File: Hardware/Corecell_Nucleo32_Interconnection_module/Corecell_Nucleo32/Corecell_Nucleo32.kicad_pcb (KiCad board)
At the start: 2 copper layers, 166.3 x 92.6 mm, 30 parts, among them IC1 PCI_EXPRESS_CARD, J1 Conn_01x19, J2 Conn_01x19, J3 Bus Standard, J4 Calculatrice_UART_groove, J5 RAK5146_UART_groove(GPS), J6 RAK5146_I2C_groove(GPS), J7 RAK5146_SPI_groove(MCU), Q1 BC548, U1 ESP32-DEVKITC-32D

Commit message: Design changed
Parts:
- moved C6 153.3 mm to (175.3, 43.9), turned to 90 degrees
- moved C2 141.3 mm to (163.0, 40.3), turned to -90 degrees
- moved C3 134.7 mm to (163.0, 48.7), turned to 90 degrees
- moved J4 127.9 mm to (184.5, 119.0), turned to 90 degrees
- moved C1 124.1 mm to (162.7, 52.3), turned to -90 degrees
- moved C8 118.6 mm to (161.5, 96.0), turned to 90 degrees
- moved R1 118.0 mm to (180.8, 78.4), turned to 90 degrees
- moved C4 116.5 mm to (175.3, 45.8), turned to -90 degrees
- moved R4 112.8 mm to (140.0, 59.9), turned to 90 degrees
- moved R8 106.4 mm to (137.1, 86.9), turned to 180 degrees
- moved R6 101.1 mm to (149.8, 102.3), turned to 90 degrees
- moved R3 92.5 mm to (172.8, 73.2), turned to 90 degrees
- moved IC1 88.9 mm to (169.3, 51.4)
- moved C5 87.1 mm to (163.0, 62.7), turned to 90 degrees
- moved R2 86.6 mm to (169.0, 69.3), turned to 90 degrees
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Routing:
- net +3V3: track 0.00 -> 46.7 mm
- net GND: track 0.00 -> 41.3 mm
- net /8: track 0.00 -> 8.50 mm
- net /5: track 0.00 -> 8.50 mm
- net /31: track 0.00 -> 8.50 mm
- net /27: track 0.00 -> 8.50 mm
- net /24: track 0.00 -> 8.50 mm
- net /12: track 0.00 -> 8.50 mm
- net /37: track 0.00 -> 8.50 mm
- net /35: track 0.00 -> 8.50 mm
- net /34: track 0.00 -> 8.50 mm
- net /18: track 0.00 -> 8.50 mm
- net /16: track 0.00 -> 8.50 mm
- net /15: track 0.00 -> 8.50 mm
- net /19: track 0.00 -> 8.50 mm
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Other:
- board text added: "NUCLEO32"
- board text added: "RAK5146"

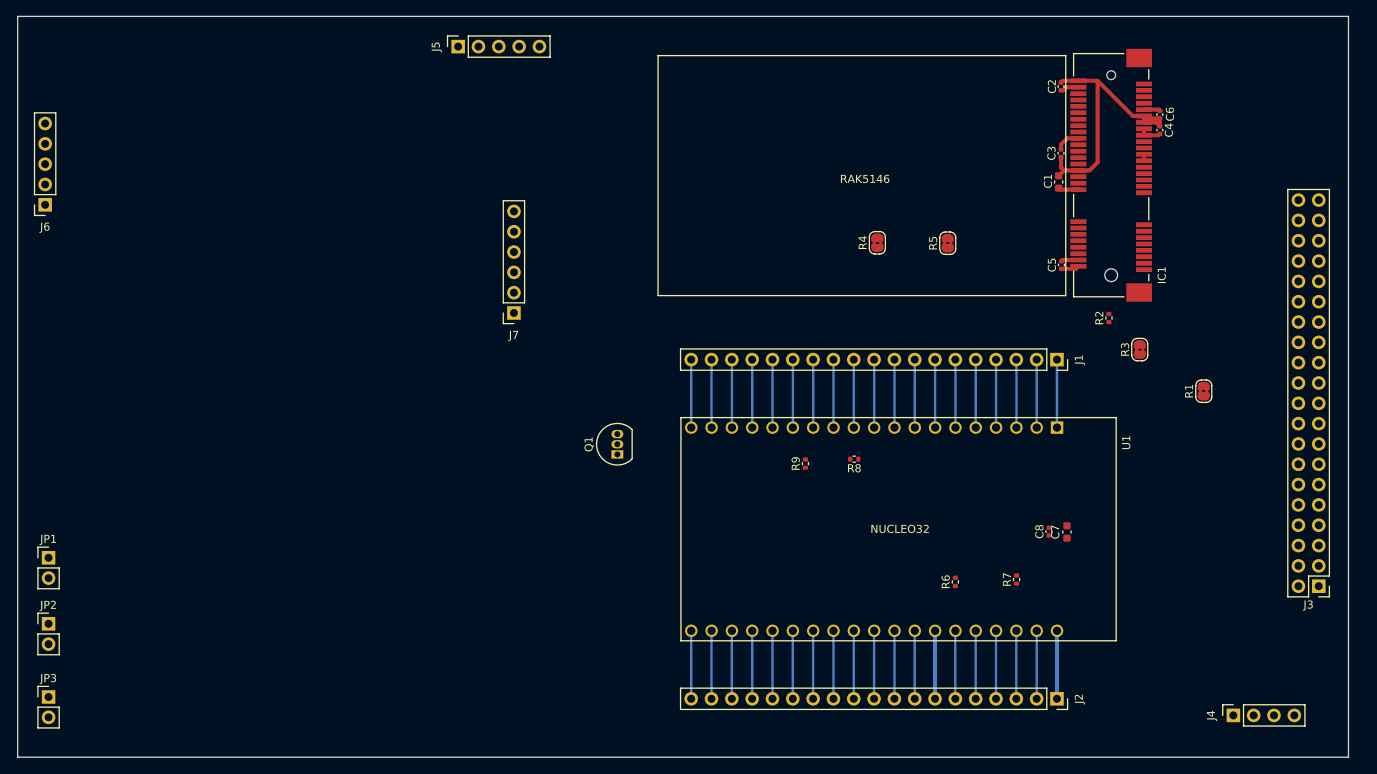
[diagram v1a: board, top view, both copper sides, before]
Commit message: Some changes in footprint and capacitors value
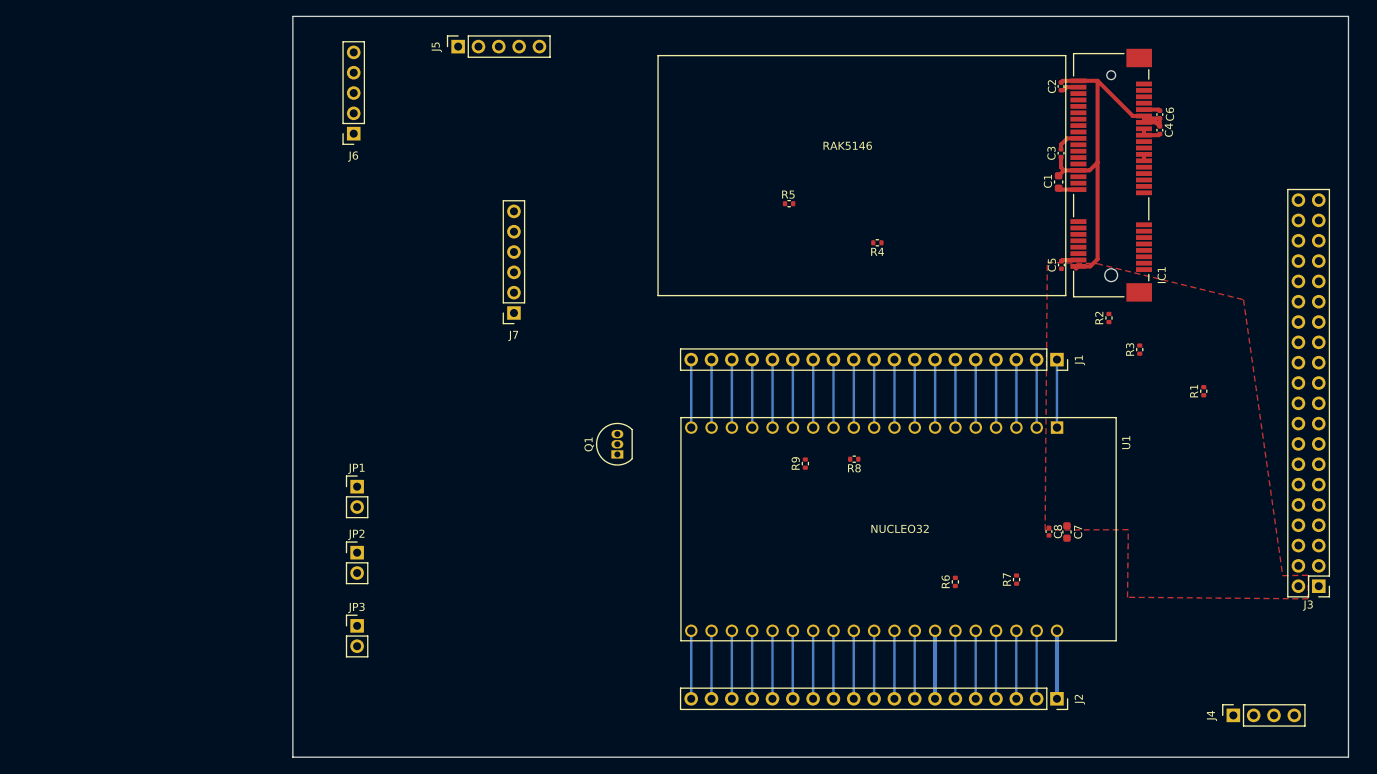
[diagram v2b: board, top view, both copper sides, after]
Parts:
- R1, R3: footprint Jumper:SolderJumper-2_P1.3mm_Bridged2Bar_RoundedPad1.0x1.5mm -> Resistor_SMD:R_0402_1005Metric
- R4, R5: value 0/NC -> 0; footprint Jumper:SolderJumper-2_P1.3mm_Bridged2Bar_RoundedPad1.0x1.5mm -> Resistor_SMD:R_0402_1005Metric
- R6, R7, R9: value 100/NC -> 100
- moved J6 39.6 mm to (74.6, 46.2)
- moved JP1 39.6 mm to (75.0, 90.4)
- moved JP2 39.6 mm to (75.0, 98.6)
- moved JP3 39.6 mm to (75.0, 107.8)
- moved R5 20.4 mm to (129.0, 55.0), turned to 180 degrees
- turned C7 to -90 degrees
- turned C8 to -90 degrees
- turned R4 to 180 degrees
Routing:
- net +3V3: track 46.7 -> 59.8 mm
- added copper zone on F.Cu, net +3V3
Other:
- board size 166.3 x 92.6 mm -> 131.9 x 92.6 mm

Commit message: Model is ready. We must revise
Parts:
- R1, R2, R4, R5: moved to B.Cu
- moved JP3 111.4 mm to (186.4, 110.2)
- moved JP1 107.2 mm to (180.4, 109.9)
- moved JP2 101.3 mm to (175.7, 109.9)
- moved J4 85.1 mm to (102.5, 96.0), turned to 0 degrees
- moved J6 51.1 mm to (102.5, 89.0)
- moved J5 40.1 mm to (102.5, 72.5), turned to 180 degrees
- moved R2 26.8 mm to (142.2, 70.9)
- moved R3 25.6 mm to (147.3, 71.4)
- moved R5 16.3 mm to (134.4, 70.4), turned to -90 degrees
- moved J7 15.8 mm to (102.5, 55.0)
- moved R8 13.4 mm to (126.9, 95.5), turned to 90 degrees
- moved R4 10.9 mm to (137.2, 70.4), turned to -90 degrees
- moved R1 5.73 mm to (186.6, 78.0)
- moved Q1 4.86 mm to (110.5, 90.2)
- moved R9 4.11 mm to (131.9, 91.5), turned to 0 degrees
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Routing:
- net /28: track 8.50 -> 230.1 mm, vias 0 -> 1
- net /21: track 8.50 -> 186.8 mm, vias 0 -> 1
- net /24: track 8.50 -> 180.1 mm, vias 0 -> 2
- net /23: track 8.50 -> 159.6 mm, vias 0 -> 1
- net /29: track 8.50 -> 154.9 mm
- net /31: track 8.50 -> 150.9 mm
- net /27: track 8.50 -> 146.4 mm, vias 0 -> 1
- net /30: track 8.50 -> 144.3 mm
- net +3V3: track 59.8 -> 176.1 mm, vias 0 -> 3
- net /8: track 8.50 -> 114.9 mm, vias 0 -> 1
- net Net-(IC1-Pad22): track 0.00 -> 91.2 mm, vias 0 -> 2
- net /6: track 8.50 -> 95.5 mm
- net /9: track 8.50 -> 84.1 mm, vias 0 -> 3
- net /22: track 8.50 -> 79.5 mm, vias 0 -> 1
- net Net-(IC1-Pad30): track 0.00 -> 68.3 mm, vias 0 -> 2
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- added copper zone on B.Cu, net GND
- added copper zone on F.Cu, net GND
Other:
- board size 131.9 x 92.6 mm -> 102 x 92.6 mm

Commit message: Silk screen is up to date
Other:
- board text added: "3V3"
- board text added: "CS"
- board text added: "GND"
- board text added: "GPS PULSE"
- board text added: "I2C GPS"
- board text added: "MISO"
- board text added: "MOSI"
- board text added: "RESET GPS"
- board text added: "RESET MCU RAK"
- board text added: "RX"
- board text added: "RX GPS"
- board text added: "SCK"
- board text added: "SCL"
- board text added: "SDA"
- board text added: "SPI MCU RAK"
- board text added: "STDBY GPS"
- board text added: "TX"
- board text added: "TX GPS"
- board text added: "UART GPS"
- board text added: "UART OBS"
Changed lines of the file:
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@@
     (property "Sheetname" "")
     (attr through_hole)
-    (fp_text reference "J4" (at 0 -2.77) (layer "F.SilkS")
+    (fp_text reference "J4" (at 0 10) (layer "F.SilkS")
       (effects (font (size 1 1) (thickness 0.15)))
     )
@@
     (property "Sheetname" "")
     (attr through_hole)
-    (fp_text reference "J5" (at 0 -2.77) (layer "F.SilkS")
+    (fp_text reference "J5" (at 0 -2.45) (layer "F.SilkS")
       (effects (font (size 1 1) (thickness 0.15)))
     )
@@
     (property "Sheetname" "")
     (attr through_hole)
-    (fp_text reference "J7" (at 0 -2.77) (layer "F.SilkS")
+    (fp_text reference "J7" (at 0 -2.5) (layer "F.SilkS")
       (effects (font (size 1 1) (thickness 0.15)))
     )
@@
     (property "Sheetname" "")
     (attr through_hole)
-    (fp_text reference "J6" (at 0 -2.77) (layer "F.SilkS")
+    (fp_text reference "J6" (at 0 -2.5) (layer "F.SilkS")
       (effects (font (size 1 1) (thickness 0.15)))
     )
@@
   (gr_rect (start 112.62 66.49) (end 163.58 36.49) (layer "F.SilkS") (width 0.15) (fill none))
   (gr_rect (start 98.42 31.59) (end 200.436 124.19) (layer "Edge.Cuts") (width 0.1) (fill none))
+  (gr_text "GPS PULSE\n" (at 106.5 81.5) (layer "F.SilkS")
+    (effects (font (size 0.5 0.5) (thickness 0.125)))
+  )
+  (gr_text "UART OBS" (at 103 108) (layer "F.SilkS")
+    (effects (font (size 1 1) (thickness 0.15)))
+  )
+  (gr_text "UART GPS\n" (at 103 76.5) (layer "F.SilkS")
+    (effects (font (size 1 1) (thickness 0.15)))
+  )
+  (gr_text "GND" (at 105 79) (layer "F.SilkS")
+    (effects (font (size 0.5 0.5) (thickness 0.125)))
+  )
+  (gr_text "SCL" (at 105 86.5) (layer "F.SilkS")
+    (effects (font (size 0.5 0.5) (thickness 0.125)))
+  )
+  (gr_text "RX" (at 105 98.5) (layer "F.SilkS")
+    (effects (font (size 0.5 0.5) (thickness 0.125)))
+  )
+  (gr_text "RX GPS" (at 106 67.5) (layer "F.SilkS")
+    (effects (font (size 0.5 0.5) (thickness 0.125)))
+  )
+  (gr_text "GND" (at 105 103.5) (layer "F.SilkS")
+    (effects (font (size 0.5 0.5) (thickness 0.125)))
+  )
+  (gr_text "STDBY GPS\n" (at 175 114.5) (layer "F.SilkS")
+    (effects (font (size 0.5 0.5) (thickness 0.125)))
+  )
   (gr_text "NUCLEO32\n" (at 142.87 95.69) (layer "F.SilkS")
     (effects (font (size 1 1) (thickness 0.15)))
   )
+  (gr_text "GND" (at 105 42.5) (layer "F.SilkS")
+    (effects (font (size 0.5 0.5) (thickness 0.125)))
+  )
+  (gr_text "3V3\n" (at 105 96) (layer "F.SilkS")
+    (effects (font (size 0.5 0.5) (thickness 0.125)))
+  )
+  (gr_text "SCK\n" (at 105 52.5) (layer "F.SilkS")
+    (effects (font (size 0.5 0.5) (thickness 0.125)))
+  )
   (gr_text "RAK5146\n" (at 136.3 47.8) (layer "F.SilkS")
     (effects (font (size 1 1) (thickness 0.15)))
   )
+  (gr_text "MISO\n" (at 105 50) (layer "F.SilkS")
+    (effects (font (size 0.5 0.5) (thickness 0.125)))
+  )
+  (gr_text "GPS PULSE\n" (at 106.5 65) (layer "F.SilkS")
+    (effects (font (size 0.5 0.5) (thickness 0.125)))
+  )
+  (gr_text "RESET GPS" (at 180.5 114.5) (layer "F.SilkS")
+    (effects (font (size 0.5 0.5) (thickness 0.125)))
+  )
+  (gr_text "3V3\n" (at 105.5 72.888944) (layer "F.SilkS")
+    (effects (font (size 0.5 0.5) (thickness 0.125)))
+  )
+  (gr_text "3V3\n" (at 105 89) (layer "F.SilkS")
+    (effects (font (size 0.5 0.5) (thickness 0.125)))
+  )
+  (gr_text "RESET MCU RAK" (at 186.4 114.5) (layer "F.SilkS")
+    (effects (font (size 0.5 0.5) (thickness 0.125)))
+  )
+  (gr_text "TX" (at 105.130233 100.79105) (layer "F.SilkS")
+    (effects (font (size 0.5 0.5) (thickness 0.125)))
+  )
+  (gr_text "SPI MCU RAK" (at 104 59) (layer "F.SilkS")
+    (effects (font (size 1 1) (thickness 0.15)))
+  )
+  (gr_text "TX GPS" (at 106 70) (layer "F.SilkS")
+    (effects (font (size 0.5 0.5) (thickness 0.125)))
+  )
+  (gr_text "GND" (at 105 62.5) (layer "F.SilkS")
+    (effects (font (size 0.5 0.5) (thickness 0.125)))
+  )
+  (gr_text "CS" (at 105 45) (layer "F.SilkS")
+    (effects (font (size 0.5 0.5) (thickness 0.125)))
+  )
+  (gr_text "MOSI" (at 105 47.5) (layer "F.SilkS")
+    (effects (font (size 0.5 0.5) (thickness 0.125)))
+  )
+  (gr_text "3V3\n" (at 105 55) (layer "F.SilkS")
+    (effects (font (size 0.5 0.5) (thickness 0.125)))
+  )
+  (gr_text "I2C GPS\n" (at 103 93) (layer "F.SilkS")
+    (effects (font (size 1 1) (thickness 0.15)))
+  )
+  (gr_text "SDA" (at 105 84) (layer "F.SilkS")
+    (effects (font (size 0.5 0.5) (thickness 0.125)))
+  )
   (segment (start 165.16 39.64) (end 166.94 39.64) (width 0.5) (layer "F.Cu") (net 1))

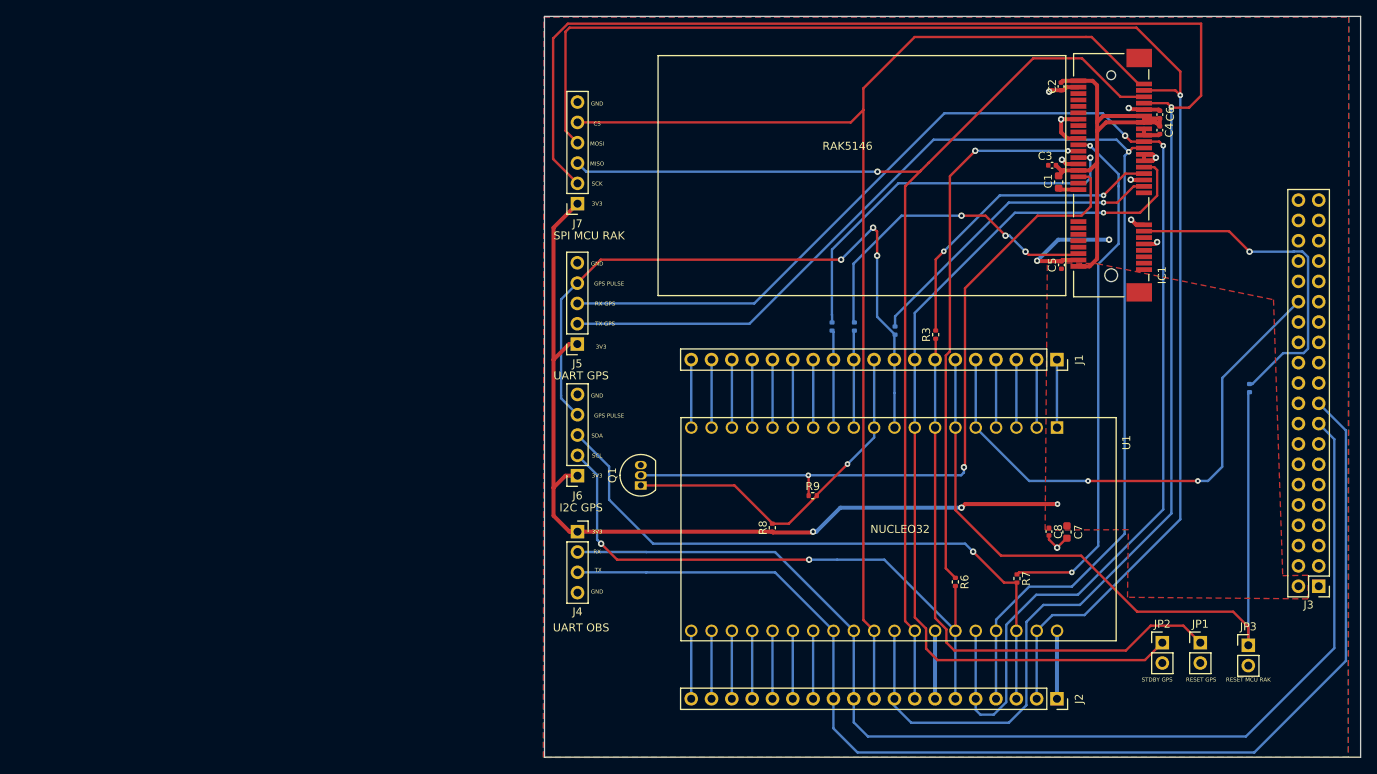
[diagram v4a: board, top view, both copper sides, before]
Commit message: mechanical dimension adjusted, routes retraced.
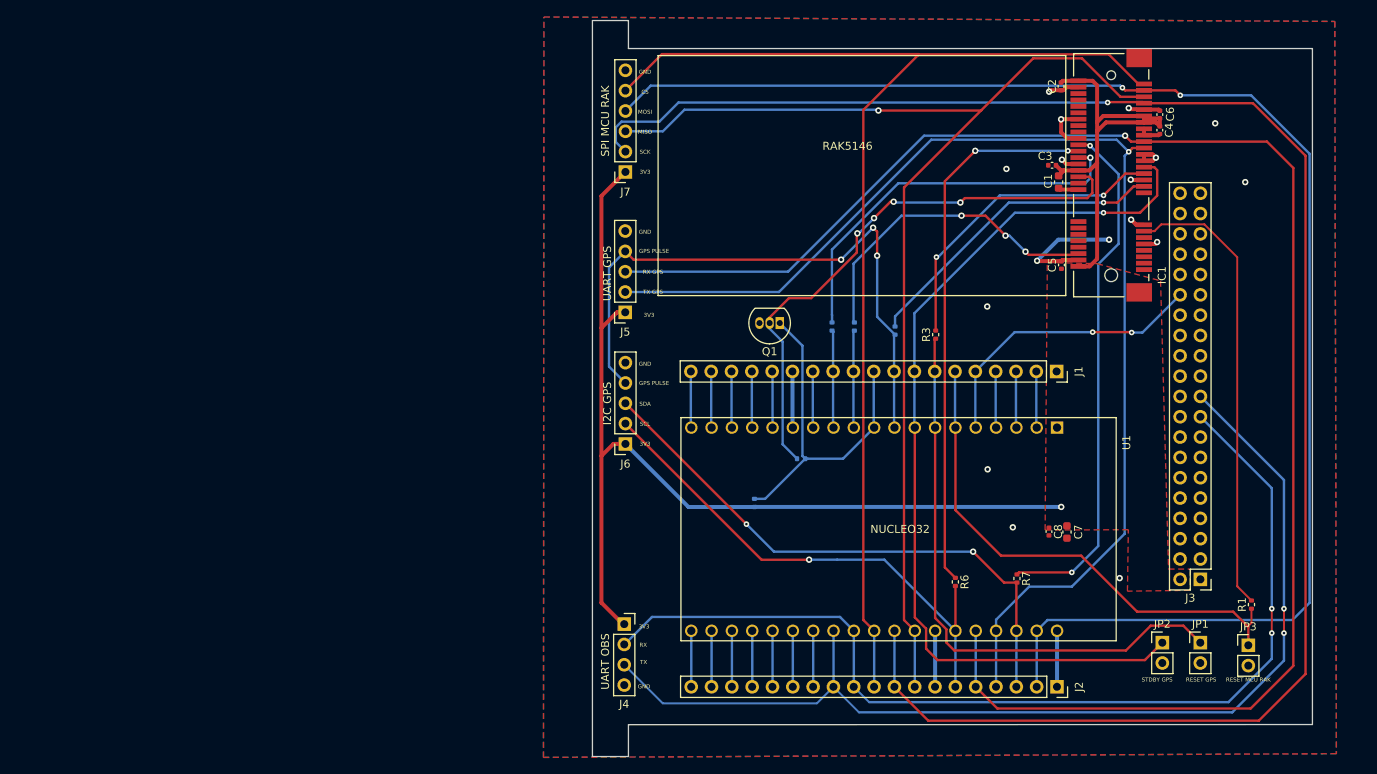
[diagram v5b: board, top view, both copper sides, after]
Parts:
- R1: moved to F.Cu
- R8, R9: moved to B.Cu
- moved R1 27.1 mm to (186.8, 105.1)
- moved Q1 26.7 mm to (127.8, 69.9), turned to 180 degrees
- moved J3 14.8 mm to (180.4, 102.0)
- moved J4 12.9 mm to (108.4, 107.6)
- moved J6 7.18 mm to (108.5, 85.0)
- moved J7 7.18 mm to (108.5, 51.0)
- moved J5 7.18 mm to (108.5, 68.6)
- moved R9 4.84 mm to (130.5, 86.9)
- moved R8 3.83 mm to (124.7, 92.4)
- moved J2 1.50 mm to (162.5, 115.4)
- moved J1 1.48 mm to (162.4, 76.0)
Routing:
- net /6: track 95.5 -> 64.7 mm
- net /5: track 67.4 -> 36.6 mm
- net /24: track 180.1 -> 204.5 mm, vias 2 -> 1
- net Net-(IC1-Pad22): track 91.2 -> 70.8 mm, vias 2 -> 4
- net /30: track 144.3 -> 127.1 mm, vias 0 -> 2
- net /31: track 150.9 -> 133.7 mm, vias 0 -> 2
- net Net-(IC1-Pad13): track 42.5 -> 57.4 mm, vias 1 -> 0
- net /25: track 75.2 -> 64.6 mm, vias 2 -> 1
- net /23: track 159.6 -> 150.4 mm
- net /28: track 230.1 -> 221.2 mm
- net /22: track 79.5 -> 71.3 mm, vias 1 -> 2
- net GND: track 74.7 -> 66.7 mm, vias 11 -> 17
- net /9: track 84.1 -> 77.4 mm
- net /29: track 154.9 -> 151.6 mm
- net +3V3: track 176.1 -> 178.8 mm, vias 3 -> 1
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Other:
- board size 102 x 92.6 mm -> 90 x 92 mm
